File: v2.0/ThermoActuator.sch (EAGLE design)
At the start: 68 parts, among them IC1 ULN2003AD, IC2 PCF8574T, U1 CD74HCT4051_D_16

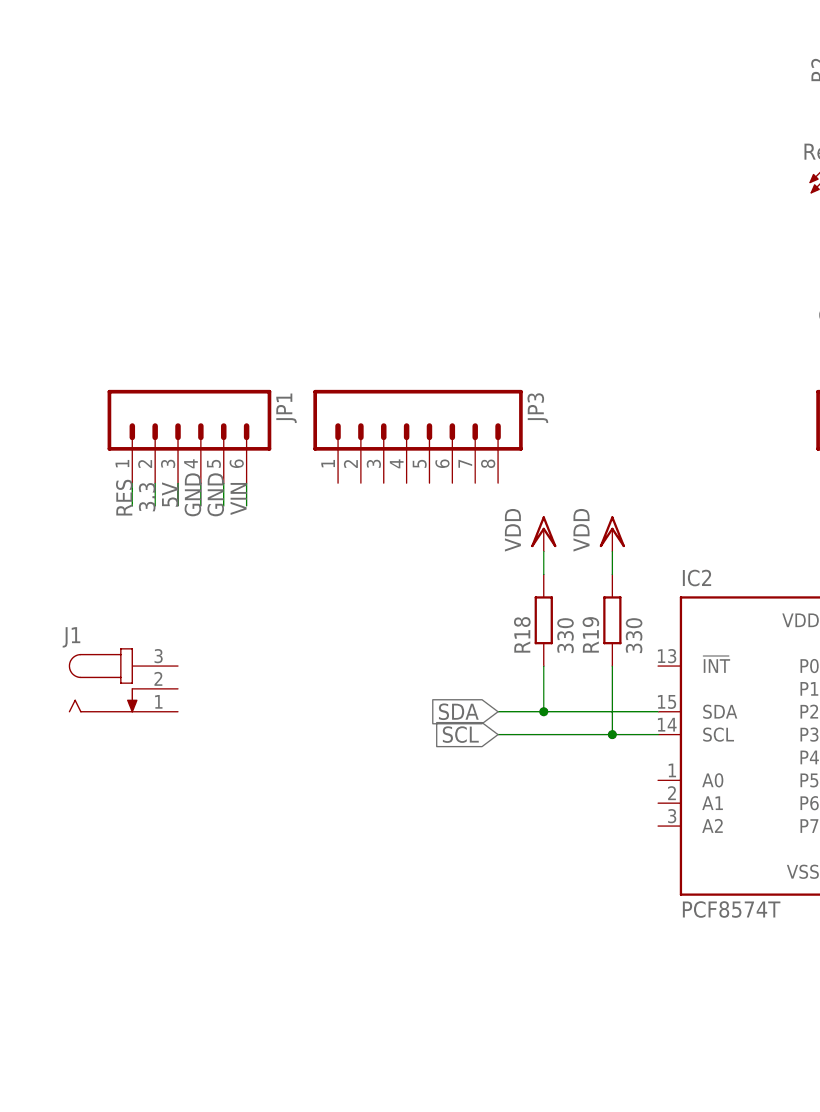
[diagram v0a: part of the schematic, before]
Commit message: PCF8574 schematics ready
schematics for the I2C GPIO expander is completed
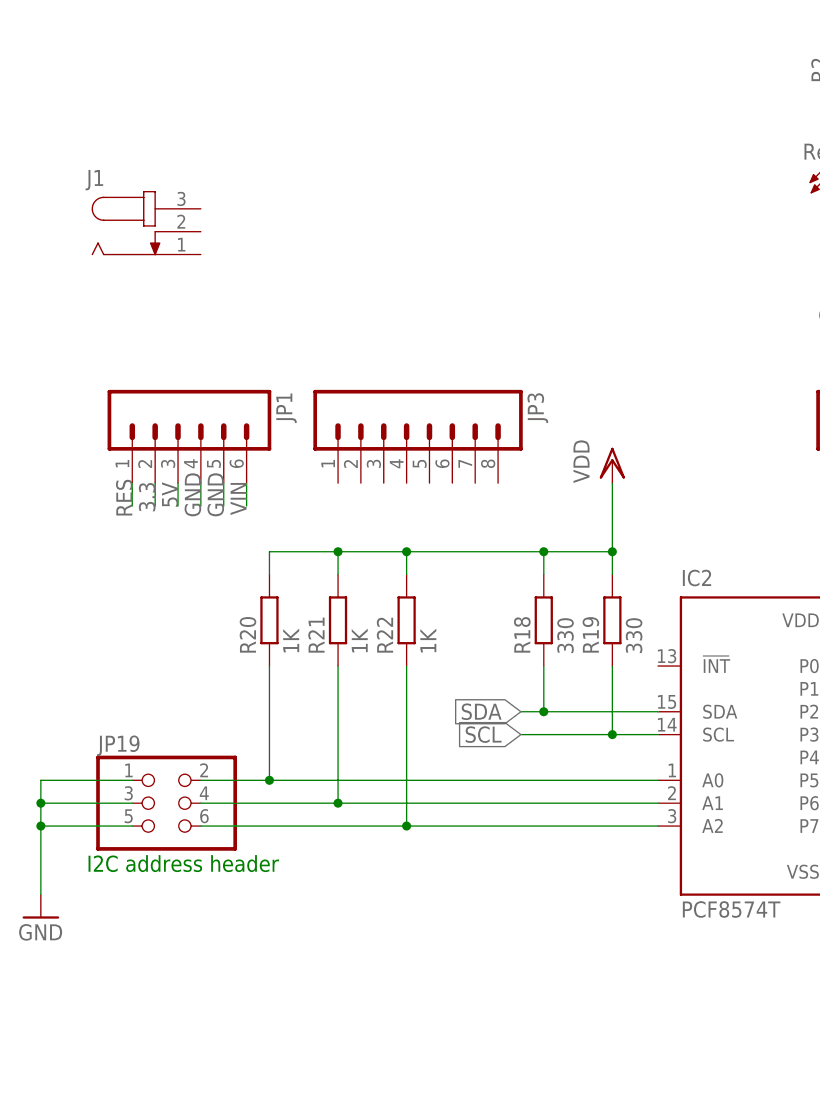
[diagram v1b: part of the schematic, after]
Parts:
- added JP19: (no value), pinhead:PINHD-2X3
- added R20, R21, R22: 1K, rcl:R-EU_R0805
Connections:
- new net N$10: IC2.A0, JP19.2, R20.1
- new net N$24: IC2.A1, JP19.4, R21.1
- new net N$25: IC2.A2, JP19.6, R22.1
- net GND: now also JP19.1, JP19.3, JP19.5
- net VDD: now also R20.2, R21.2, R22.2
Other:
- note added: "I2C address header"
- moved on the sheet: J1
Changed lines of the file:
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@@
 <?xml version="1.0" encoding="utf-8"?>
 <!DOCTYPE eagle SYSTEM "eagle.dtd">
-<eagle version="7.1.0">
+<eagle version="7.4.0">
 <drawing>
 <settings>
@@
 <part name="R19" library="rcl" deviceset="R-EU_" device="R0805" value="330"/>
 <part name="VDD9" library="supply1" deviceset="VDD" device=""/>
-<part name="VDD10" library="supply1" deviceset="VDD" device=""/>
 <part name="VDD11" library="supply1" deviceset="VDD" device=""/>
 <part name="GND29" library="SparkFun" deviceset="GND" device=""/>
+<part name="JP19" library="pinhead" deviceset="PINHD-2X3" device=""/>
+<part name="GND30" library="SparkFun" deviceset="GND" device=""/>
+<part name="R20" library="rcl" deviceset="R-EU_" device="R0805" value="1K"/>
+<part name="R21" library="rcl" deviceset="R-EU_" device="R0805" value="1K"/>
+<part name="R22" library="rcl" deviceset="R-EU_" device="R0805" value="1K"/>
 </parts>
 <sheets>
 <sheet>
 <plain>
+<text x="12.7" y="10.16" size="1.778" layer="91">I2C address header</text>
 </plain>
 <instances>
@@
 <instance part="JP-8" gate="G$1" x="271.78" y="-10.16"/>
 <instance part="U$1" gate="G$1" x="378.46" y="106.68"/>
-<instance part="J1" gate="G$1" x="17.78" y="30.48"/>
+<instance part="J1" gate="G$1" x="20.32" y="81.28"/>
 <instance part="R18" gate="G$1" x="63.5" y="38.1" rot="R90"/>
 <instance part="R19" gate="G$1" x="71.12" y="38.1" rot="R90"/>
-<instance part="VDD9" gate="G$1" x="71.12" y="48.26"/>
-<instance part="VDD10" gate="G$1" x="63.5" y="48.26"/>
+<instance part="VDD9" gate="G$1" x="71.12" y="55.88"/>
 <instance part="VDD11" gate="G$1" x="101.6" y="48.26"/>
 <instance part="GND29" gate="1" x="101.6" y="5.08"/>
+<instance part="JP19" gate="A" x="20.32" y="17.78"/>
+<instance part="GND30" gate="1" x="7.62" y="5.08"/>
+<instance part="R20" gate="G$1" x="33.02" y="38.1" rot="R90"/>
+<instance part="R21" gate="G$1" x="40.64" y="38.1" rot="R90"/>
+<instance part="R22" gate="G$1" x="48.26" y="38.1" rot="R90"/>
 </instances>
 <busses>
@@
 <wire x1="101.6" y1="10.16" x2="101.6" y2="7.62" width="0.1524" layer="91"/>
 </segment>
+<segment>
+<pinref part="JP19" gate="A" pin="1"/>
+<pinref part="GND30" gate="1" pin="GND"/>
+<wire x1="17.78" y1="20.32" x2="7.62" y2="20.32" width="0.1524" layer="91"/>
+<wire x1="7.62" y1="20.32" x2="7.62" y2="17.78" width="0.1524" layer="91"/>
+<pinref part="JP19" gate="A" pin="3"/>
+<wire x1="7.62" y1="17.78" x2="7.62" y2="15.24" width="0.1524" layer="91"/>
+<wire x1="7.62" y1="15.24" x2="7.62" y2="7.62" width="0.1524" layer="91"/>
+<wire x1="17.78" y1="17.78" x2="7.62" y2="17.78" width="0.1524" layer="91"/>
+<junction x="7.62" y="17.78"/>
+<pinref part="JP19" gate="A" pin="5"/>
+<wire x1="17.78" y1="15.24" x2="7.62" y2="15.24" width="0.1524" layer="91"/>
+<junction x="7.62" y="15.24"/>
+</segment>
 </net>
 <net name="VIN" class="0">
@@
 <pinref part="IC2" gate="G$1" pin="SDA"/>
 <wire x1="76.2" y1="27.94" x2="63.5" y2="27.94" width="0.1524" layer="91"/>
-<label x="58.42" y="27.94" size="1.778" layer="95" rot="R180" xref="yes"/>
+<label x="60.96" y="27.94" size="1.778" layer="95" rot="R180" xref="yes"/>
 <pinref part="R18" gate="G$1" pin="1"/>
-<wire x1="63.5" y1="27.94" x2="58.42" y2="27.94" width="0.1524" layer="91"/>
+<wire x1="63.5" y1="27.94" x2="60.96" y2="27.94" width="0.1524" layer="91"/>
 <wire x1="63.5" y1="33.02" x2="63.5" y2="27.94" width="0.1524" layer="91"/>
 <junction x="63.5" y="27.94"/>
@@
 <pinref part="IC2" gate="G$1" pin="SCL"/>
 <wire x1="76.2" y1="25.4" x2="71.12" y2="25.4" width="0.1524" layer="91"/>
-<label x="58.42" y="25.4" size="1.778" layer="95" rot="R180" xref="yes"/>
+<label x="60.96" y="25.4" size="1.778" layer="95" rot="R180" xref="yes"/>
 <pinref part="R19" gate="G$1" pin="1"/>
-<wire x1="71.12" y1="25.4" x2="58.42" y2="25.4" width="0.1524" layer="91"/>
+<wire x1="71.12" y1="25.4" x2="60.96" y2="25.4" width="0.1524" layer="91"/>
 <wire x1="71.12" y1="33.02" x2="71.12" y2="25.4" width="0.1524" layer="91"/>
 <junction x="71.12" y="25.4"/>
@@
 <wire x1="71.12" y1="43.18" x2="71.12" y2="45.72" width="0.1524" layer="91"/>
 <pinref part="VDD9" gate="G$1" pin="VDD"/>
-</segment>
-<segment>
+<pinref part="R20" gate="G$1" pin="2"/>
+<wire x1="71.12" y1="45.72" x2="71.12" y2="53.34" width="0.1524" layer="91"/>
+<wire x1="33.02" y1="43.18" x2="33.02" y2="45.72" width="0.1524" layer="91"/>
+<pinref part="R21" gate="G$1" pin="2"/>
+<wire x1="40.64" y1="43.18" x2="40.64" y2="45.72" width="0.1524" layer="91"/>
+<wire x1="33.02" y1="45.72" x2="40.64" y2="45.72" width="0.1524" layer="91"/>
+<pinref part="R22" gate="G$1" pin="2"/>
+<wire x1="48.26" y1="43.18" x2="48.26" y2="45.72" width="0.1524" layer="91"/>
+<wire x1="40.64" y1="45.72" x2="48.26" y2="45.72" width="0.1524" layer="91"/>
+<junction x="40.64" y="45.72"/>
 <pinref part="R18" gate="G$1" pin="2"/>
 <wire x1="63.5" y1="43.18" x2="63.5" y2="45.72" width="0.1524" layer="91"/>
-<pinref part="VDD10" gate="G$1" pin="VDD"/>
+<wire x1="48.26" y1="45.72" x2="63.5" y2="45.72" width="0.1524" layer="91"/>
+<junction x="48.26" y="45.72"/>
+<wire x1="63.5" y1="45.72" x2="71.12" y2="45.72" width="0.1524" layer="91"/>
+<junction x="63.5" y="45.72"/>
+<junction x="71.12" y="45.72"/>
 </segment>
 <segment>
@@
 </segment>
 </net>
+<net name="N$10" class="0">
+<segment>
+<pinref part="JP19" gate="A" pin="2"/>
+<pinref part="IC2" gate="G$1" pin="A0"/>
+<wire x1="25.4" y1="20.32" x2="33.02" y2="20.32" width="0.1524" layer="91"/>
+<pinref part="R20" gate="G$1" pin="1"/>
+<wire x1="33.02" y1="20.32" x2="76.2" y2="20.32" width="0.1524" layer="91"/>
+<wire x1="33.02" y1="33.02" x2="33.02" y2="20.32" width="0.1524" layer="91"/>
+<junction x="33.02" y="20.32"/>
+</segment>
+</net>
+<net name="N$24" class="0">
+<segment>
+<pinref part="JP19" gate="A" pin="4"/>
+<pinref part="IC2" gate="G$1" pin="A1"/>
+<wire x1="25.4" y1="17.78" x2="40.64" y2="17.78" width="0.1524" layer="91"/>
+<pinref part="R21" gate="G$1" pin="1"/>
+<wire x1="40.64" y1="17.78" x2="76.2" y2="17.78" width="0.1524" layer="91"/>
+<wire x1="40.64" y1="33.02" x2="40.64" y2="17.78" width="0.1524" layer="91"/>
+<junction x="40.64" y="17.78"/>
+</segment>
+</net>
+<net name="N$25" class="0">
+<segment>
+<pinref part="JP19" gate="A" pin="6"/>
+<pinref part="IC2" gate="G$1" pin="A2"/>
+<wire x1="25.4" y1="15.24" x2="48.26" y2="15.24" width="0.1524" layer="91"/>
+<pinref part="R22" gate="G$1" pin="1"/>
+<wire x1="48.26" y1="15.24" x2="76.2" y2="15.24" width="0.1524" layer="91"/>
+<wire x1="48.26" y1="33.02" x2="48.26" y2="15.24" width="0.1524" layer="91"/>
+<junction x="48.26" y="15.24"/>
+</segment>
+</net>

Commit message: 8ch mux routing complete
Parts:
- removed R11: 100K, rcl:R-EU_R0805
- added JP20: (no value), pinhead:PINHD-2X8
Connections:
- new net N$26: JP20.1, JP3.1
- new net N$27: JP20.3, JP3.2
- new net N$28: JP20.5, JP3.3
- new net N$29: JP20.7, JP3.4
- new net N$30: JP20.9, JP3.5
- new net N$31: JP20.11, JP3.6
- new net N$36: JP20.10, JP20.12, JP20.14, JP20.16, JP20.2, JP20.4, JP20.6, JP20.8, U1.A
- new net N$37: JP20.13, JP3.7
- new net N$38: JP20.15, JP3.8
- net D5: now also U1.S0
- net D6: now also U1.S1
- net D7: now also U1.S2
- net GND: now also U1.*E, U1.GND, U1.VEE
- net VDD: now also U1.VCC; no longer R11.2
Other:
- note added: "8ch Multiplexer"
- note added: "Analog Input Selector (use one strap only)"
- note added: "Darlington Transistor Array"
- note added: "I2C GPIO Expander"
- note added: "switch control"
- moved on the sheet: C1, C2, C3, C4, C5, C6, C7, C8, JP-1, JP-2, JP-3, JP-4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

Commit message: PCB caped for lower profile
two capes are cut. All components are thrown on the PCB
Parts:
- removed JP-1, JP-2, JP-3, JP-4, JP-5, JP-6, JP-7, JP-8: M025MM, SparkFun-Connectors:M025MM
- removed LED10: Blue, led:LEDCHIP-LED0805
- removed R27: 330, rcl:R-EU_R0805
- removed U$1: ESP8266-07, lio:ESP8266-07
- added C10, C13, C9: 100nF, rcl:C-EUC0805
- added C11, C12: 5uF, SparkFun-Capacitors:CAP_POL1206
- added IC3: REG1117, burr-brown:REG1117
- added JP21, JP22, JP23, JP24: M025MM, SparkFun-Connectors:M025MM
- added JP25, JP28: (no value), SparkFun:M02LOCK
- added JP26, JP27: M16LOCK, SparkFun:M16LOCK
- added LED2: White, led:LEDCHIP-LED0805
- added MISHA1: ESP8266-07, lio:ESP8266-07
- added Q1, Q2: 200mA/50V, SparkFun-DiscreteSemi:MOSFET-NCHANNELBSS138
- added R11: 1K, rcl:R-EU_R1206
- added R23, R24, R25, R26: 10K, rcl:R-EU_R0805
- IC1: value ULN2003AD -> PCF8574T; device uln-udn:ULN2003AD -> micro-philips:PCF8574T
- IC2: value PCF8574T -> ULN2003AD; device micro-philips:PCF8574T -> uln-udn:ULN2003AD
- JP1: value (none) -> M025MM; device SparkFun:M06LOCK -> SparkFun-Connectors:M025MM
- JP10, JP8: value M025MM -> (none); device SparkFun-Connectors:M025MM -> SparkFun:M08LOCK
- JP15: device SparkFun:M02LOCK -> SparkFun:M08LOCK
- JP16: value M16LOCK -> (none); device SparkFun:M16LOCK -> SparkFun:M08LOCK
- JP17: value M16LOCK -> M025MM; device SparkFun:M16LOCK -> SparkFun-Connectors:M025MM
- JP18: value (none) -> M025MM; device SparkFun:M02LOCK -> SparkFun-Connectors:M025MM
- JP19: value (none) -> M025MM; device pinhead:PINHD-2X3 -> SparkFun-Connectors:M025MM
- JP2: value M10LOCK -> M025MM; device SparkFun-Connectors:M10LOCK -> SparkFun-Connectors:M025MM
- JP20: value (none) -> M025MM; device pinhead:PINHD-2X8 -> SparkFun-Connectors:M025MM
- JP3, JP4: value (none) -> M025MM; device SparkFun:M08LOCK -> SparkFun-Connectors:M025MM
- JP5: device SparkFun:M08LOCK -> pinhead:PINHD-2X3
- JP6: value (none) -> M10LOCK; device SparkFun:M08LOCK -> SparkFun-Connectors:M10LOCK
- JP7: value M025MM -> (none); device SparkFun-Connectors:M025MM -> SparkFun:M06LOCK
- JP9: value M025MM -> (none); device SparkFun-Connectors:M025MM -> pinhead:PINHD-2X8
- LED1: value Red -> White
- LED3, LED4, LED5, LED6, LED7, LED8: value Blue -> White
- R10, R2, R4: value 330 -> 1K; device rcl:R-EU_R0805 -> rcl:R-EU_R1206
- R14, R15, R16, R17: value 1K -> 3K3; device rcl:R-EU_R1206 -> rcl:R-EU_R0805
- R18, R19: value 330 -> 3K3
- R20, R21, R22: value 1K -> 3K3
- R5, R6, R7: value 330 -> 1K
- R8, R9: value 330 -> 4K7
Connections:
- removed net D16: JP5.6
- removed net D17: JP5.5
- removed net D18: JP5.4
- removed net D19: JP5.3
- removed net GND: C1.-, C2.-, C3.-, C4.-, C5.-, C6.-, C7.-, C8.-, IC1.GND, IC2.VSS, JP-1.1, JP-2.1, JP-3.1, JP-4.1, JP-5.1, JP-6.1, JP-7.1, JP-8.1, JP1.4, JP1.5, JP14.1, JP18.1, JP18.2, JP19.1, JP19.3, JP19.5, JP2.7, LED1.C, U1.*E, U1.GND, U1.VEE
- new net 3V3: C12.+, C13.1, IC3.VOUT, MISHA1.CH_PD, MISHA1.REST, MISHA1.VCC, Q1.G, Q2.G, R23.2, R24.2
- new net N$40: MISHA1.TXD, Q1.S, R23.1
- new net N$41: MISHA1.RXD, Q2.S, R24.1
- new net NNN: C1.-, C10.2, C11.-, C12.-, C13.2, C2.-, C3.-, C4.-, C5.-, C6.-, C7.-, C8.-, C9.2, IC1.VSS, IC2.GND, IC3.GND, J1.1, JP1.1, JP11.1, JP12.1, JP13.1, JP14.1, JP2.1, JP24.1, JP28.1, JP28.2, JP3.1, JP4.1, JP5.1, JP5.3, JP5.5, JP6.7, JP7.4, JP7.5, LED9.C, MISHA1.GND, U1.*E, U1.GND, U1.VEE
- new net RX1: JP16.3
- new net RX2: JP16.5, Q1.D, R25.1
- new net TX0: JP10.2
- new net TX2: JP16.6, Q2.D, R26.1
- net 3.3: now also JP7.2; no longer JP1.2
- net 5V: now also JP7.3; no longer JP1.3
- net AO0: now also IC2.O1, JP17.2, LED1.C; no longer IC1.O1, JP7.2, LED3.C
- net AO1: now also IC2.O2, JP18.2, LED2.C; no longer IC1.O2, JP8.2, LED4.C
- net AO2: now also IC2.O3, JP19.2, LED3.C; no longer IC1.O3, JP9.2, LED5.C
- net AO3: now also IC2.O4, JP20.2, LED4.C; no longer IC1.O4, JP10.2, LED6.C
- net AO4: now also IC2.O5, JP21.2, LED5.C; no longer IC1.O5, JP11.2, LED7.C
- net AO5: now also IC2.O6, JP22.2, LED6.C; no longer IC1.O6, JP12.2, LED8.C
- net AO6: now also IC2.O7, JP23.2, LED7.C; no longer IC1.O7, JP13.2, LED9.C
- net AO7: now also IC1.P7, JP24.2, LED8.C; no longer JP14.2, LED10.C
- net AREF: now also JP6.8; no longer JP2.8
- net AS0: now also R1.2; no longer R15.2
- net AS1: now also R2.2; no longer R1.2
- net AS3: now also R4.2; no longer R12.2
- net AS4: now also R10.2; no longer R13.2
- net AS5: now also R11.2; no longer R14.2
- net AS6: now also R12.2; no longer R16.2
- net AS7: now also R13.2; no longer R17.2
- net D10: now also JP6.3, U1.S2; no longer JP2.3
- net D11: now also JP6.4; no longer JP2.4
- net D12: now also JP6.5; no longer JP2.5
- net D13: now also JP6.6; no longer JP2.6
- net D14: now also JP16.8; no longer JP5.8
- net D15: now also JP16.7; no longer JP5.7
- net D2: now also JP10.3; no longer JP4.3
- net D22: now also JP27.1; no longer JP17.1
- net D23: now also JP26.16; no longer JP16.16
- net D24: now also JP27.2; no longer JP17.2
- net D25: now also JP26.15; no longer JP16.15
- net D26: now also JP27.3; no longer JP17.3
- net D27: now also JP26.14; no longer JP16.14
- net D28: now also JP27.4; no longer JP17.4
- net D29: now also JP26.13; no longer JP16.13
- net D3: now also JP10.4; no longer JP4.4
- net D30: now also JP27.5; no longer JP17.5
- net D31: now also JP26.12; no longer JP16.12
- net D32: now also JP27.6; no longer JP17.6
- net D33: now also JP26.11; no longer JP16.11
- net D34: now also JP27.7; no longer JP17.7
- net D35: now also JP26.10; no longer JP16.10
- net D36: now also JP27.8; no longer JP17.8
- net D37: now also JP26.9; no longer JP16.9
- net D38: now also JP27.9; no longer JP17.9
- net D39: now also JP26.8; no longer JP16.8
- net D4: now also JP10.5; no longer JP4.5
- net D40: now also JP27.10; no longer JP17.10
- net D41: now also JP26.7; no longer JP16.7
- net D42: now also JP27.11; no longer JP17.11
- net D43: now also JP26.6; no longer JP16.6
- net D44: now also JP27.12; no longer JP17.12
- net D45: now also JP26.5; no longer JP16.5
- net D46: now also JP27.13; no longer JP17.13
- net D47: now also JP26.4; no longer JP16.4
- net D48: now also JP27.14; no longer JP17.14
- net D49: now also JP26.3; no longer JP16.3
- net D5: now also JP10.6; no longer JP4.6, U1.S0
- net D50: now also JP27.15; no longer JP17.15
- net D51: now also JP26.2; no longer JP16.2
- net D52: now also JP27.16; no longer JP17.16
- net D53: now also JP26.1; no longer JP16.1
- net D6: now also JP10.7; no longer JP4.7, U1.S1
- net D7: now also JP10.8; no longer JP4.8, U1.S2
- net D8: now also JP6.1, U1.S0; no longer JP2.1
- net D9: now also JP6.2, U1.S1; no longer JP2.2
- net N$1: now also JP1.2, R1.1; no longer JP-1.2, R15.1
- net N$10: now also IC1.A0, JP5.2, R5.1; no longer IC2.A0, JP19.2, R20.1
- net N$11: now also JP3.2; no longer JP-3.2
- net N$12: now also JP4.2, R4.1; no longer JP-4.2, R12.1
- net N$126: now also LED9.A, R22.1; no longer LED1.A, R2.1
- net N$13: now also LED1.A, R14.1; no longer LED3.A, R4.1
- net N$14: now also LED2.A, R15.1; no longer LED4.A, R5.1
- net N$15: now also LED3.A, R16.1; no longer LED5.A, R6.1
- net N$16: now also LED4.A, R17.1; no longer LED6.A, R7.1
- net N$17: now also LED5.A, R18.1; no longer LED7.A, R8.1
- net N$18: now also LED6.A, R19.1; no longer LED8.A, R9.1
- net N$19: now also LED7.A, R20.1; no longer LED9.A, R10.1
- net N$2: now also JP2.2, R2.1; no longer JP-2.2, R1.1
- net N$20: now also JP11.2, R10.1; no longer JP-5.2, R13.1
- net N$21: now also JP12.2, R11.1; no longer JP-6.2, R14.1
- net N$22: now also JP13.2, R12.1; no longer JP-7.2, R16.1
- net N$23: now also JP14.2, R13.1; no longer JP-8.2, R17.1
- net N$24: now also IC1.A1, JP5.4, R6.1; no longer IC2.A1, JP19.4, R21.1
- net N$25: now also IC1.A2, JP5.6, R7.1; no longer IC2.A2, JP19.6, R22.1
- net N$26: now also JP8.1, JP9.1; no longer JP20.1, JP3.1
- net N$27: now also JP8.2, JP9.3; no longer JP20.3, JP3.2
- net N$28: now also JP8.3, JP9.5; no longer JP20.5, JP3.3
- net N$29: now also JP8.4, JP9.7; no longer JP20.7, JP3.4
- net N$3: now also IC1.P0, IC2.I1; no longer IC1.I1, IC2.P0
- net N$30: now also JP8.5, JP9.9; no longer JP20.9, JP3.5
- net N$31: now also JP8.6, JP9.11; no longer JP20.11, JP3.6
- net N$32: now also LED8.A, R21.1; no longer LED10.A, R27.1
- net N$36: now also JP9.10, JP9.12, JP9.14, JP9.16, JP9.2, JP9.4, JP9.6, JP9.8; no longer JP20.10, JP20.12, JP20.14, JP20.16, JP20.2, JP20.4, JP20.6, JP20.8
- net N$37: now also JP8.7, JP9.13; no longer JP20.13, JP3.7
- net N$38: now also JP8.8, JP9.15; no longer JP20.15, JP3.8
- net N$4: now also IC1.P1, IC2.I2; no longer IC1.I2, IC2.P1
- net N$5: now also IC1.P2, IC2.I3; no longer IC1.I3, IC2.P2
- net N$6: now also IC1.P3, IC2.I4; no longer IC1.I4, IC2.P3
- net N$7: now also IC1.P4, IC2.I5; no longer IC1.I5, IC2.P4
- net N$8: now also IC1.P5, IC2.I6; no longer IC1.I6, IC2.P5
- net N$9: now also IC1.P6, IC2.I7; no longer IC1.I7, IC2.P6
- net RES: now also JP7.1; no longer JP1.1
- net RX0: now also JP10.1; no longer JP4.1
- net SCL: now also IC1.SCL, JP16.1, R9.1; no longer IC2.SCL, JP5.1, R19.1
- net SDA: now also IC1.SDA, JP16.2, R8.1; no longer IC2.SDA, JP5.2, R18.1
- net TX1: now also JP16.4; no longer JP4.2
- net VDD: now also C10.1, C11.+, C9.1, IC1.VDD, IC2.CD+, IC3.VIN, J1.3, JP17.1, JP18.1, JP19.1, JP20.1, JP21.1, JP22.1, JP23.1, JP25.1, JP25.2, R14.2, R15.2, R16.2, R17.2, R25.2, R26.2; no longer IC1.CD+, IC2.VDD, JP10.1, JP11.1, JP12.1, JP13.1, JP15.1, JP15.2, JP7.1, JP8.1, JP9.1, R10.2, R2.2, R27.2, R4.2
- net VIN: now also JP7.6; no longer JP1.6
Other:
- note added: "* R18 and R19 are populated on the master board only"
- note added: "All the pins on JP4 and JP17 headers are reserved for the LCD touch screen"
- note added: "Components on this sheet are populated on the master board only"
- note added: "Level shifter"
- note added: "Not all slave boards require individual power supply. The power to slave is provided through the pin headers. Consider the total power budget. Count about 1A per slave board plus 1.5A for the master board"
- note added: "Power LED"
- note added: "Relay control LEDs"
- note added: "The board uses individual 3V3 regulator, since the 3V3 from the mother board may not meet the power requirements of the WiFi module"
- note added: "WiFi Module ESP07"
- moved on the sheet: JP11, JP12, JP13, JP14, JP18, LED1, LED3, LED4, LED5, LED6, LED7, LED8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

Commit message: to the fab
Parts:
- removed JP17, JP18, JP19, JP20, JP21, JP22: M025MM, SparkFun-Connectors:M025MM
- added C14: 100nF, rcl:C-EUC0805
- added D1: 1N4001, diode:DIODE-D-10
- added R27: 10K, resistor:R-EU_R0805
- added X1: (no value), con-phoenix-500:MSTBV8
- 1, 2, 3, 4, 5, 6, 7, 8: value White -> (none)
- renumbered LED1 to 1, LED2 to 2, LED3 to 3, LED4 to 4, LED5 to 5, LED6 to 6, LED7 to 7, LED8 to 8
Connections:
- removed net NNN: C1.-, C10.2, C11.-, C12.-, C13.2, C2.-, C3.-, C4.-, C5.-, C6.-, C7.-, C8.-, C9.2, IC1.VSS, IC2.GND, IC3.GND, J1.1, JP1.1, JP11.1, JP12.1, JP13.1, JP14.1, JP2.1, JP24.1, JP28.1, JP28.2, JP3.1, JP4.1, JP5.1, JP5.3, JP5.5, JP6.7, JP7.4, JP7.5, LED9.C, MISHA1.GND, U1.*E, U1.GND, U1.VEE
- new net GND: C1.-, C10.2, C11.-, C12.-, C13.2, C14.2, C2.-, C3.-, C4.-, C5.-, C6.-, C7.-, C8.-, C9.2, IC1.VSS, IC2.GND, IC3.GND, J1.1, JP1.1, JP11.1, JP12.1, JP13.1, JP14.1, JP2.1, JP24.1, JP24.2, JP28.1, JP28.2, JP3.1, JP4.1, JP5.1, JP5.3, JP5.5, JP6.7, JP7.4, JP7.5, LED9.C, MISHA1.GND, U1.*E, U1.GND, U1.VEE
- new net N$42: D1.A, J1.3
- net AO0: now also X1-8.SK; no longer JP17.2
- net AO1: now also X1-7.SK; no longer JP18.2
- net AO2: now also X1-6.SK; no longer JP19.2
- net AO3: now also X1-5.SK; no longer JP20.2
- net AO4: now also X1-4.SK; no longer JP21.2
- net AO5: now also X1-3.SK; no longer JP22.2
- net AO6: now also X1-2.SK; no longer JP23.2
- net AO7: now also X1-1.SK; no longer JP24.2
- net N$36: now also R27.1
- net VDD: now also C14.1, D1.C, JP23.2, R27.2; no longer J1.3, JP17.1, JP18.1, JP19.1, JP20.1, JP21.1, JP22.1
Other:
- note added: "LED1"
- note added: "LED8"
- note added: "Voltage Divider 1% precision or better"
- moved on the sheet: JP8, JP9
